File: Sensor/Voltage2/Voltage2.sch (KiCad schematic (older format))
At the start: 31 parts, among them J1 Conn_01x03_Female, J2 STX-3120-5B, J3 Conn_01x04_Female, T1 Transformer_1P_1S, U1 OPA4134

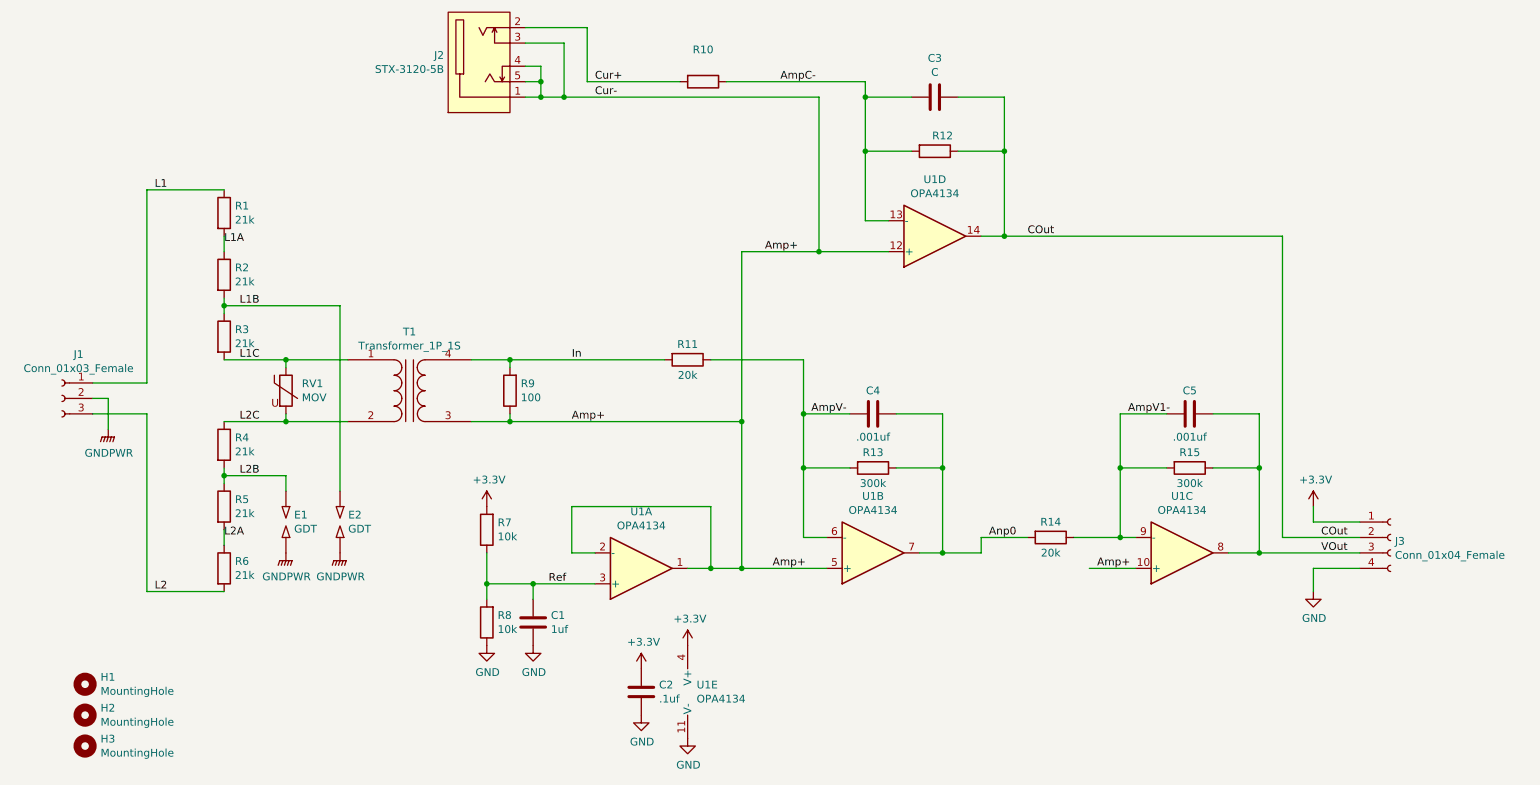
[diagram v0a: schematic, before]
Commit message: Fix footprint.  Fix wiring for connector.
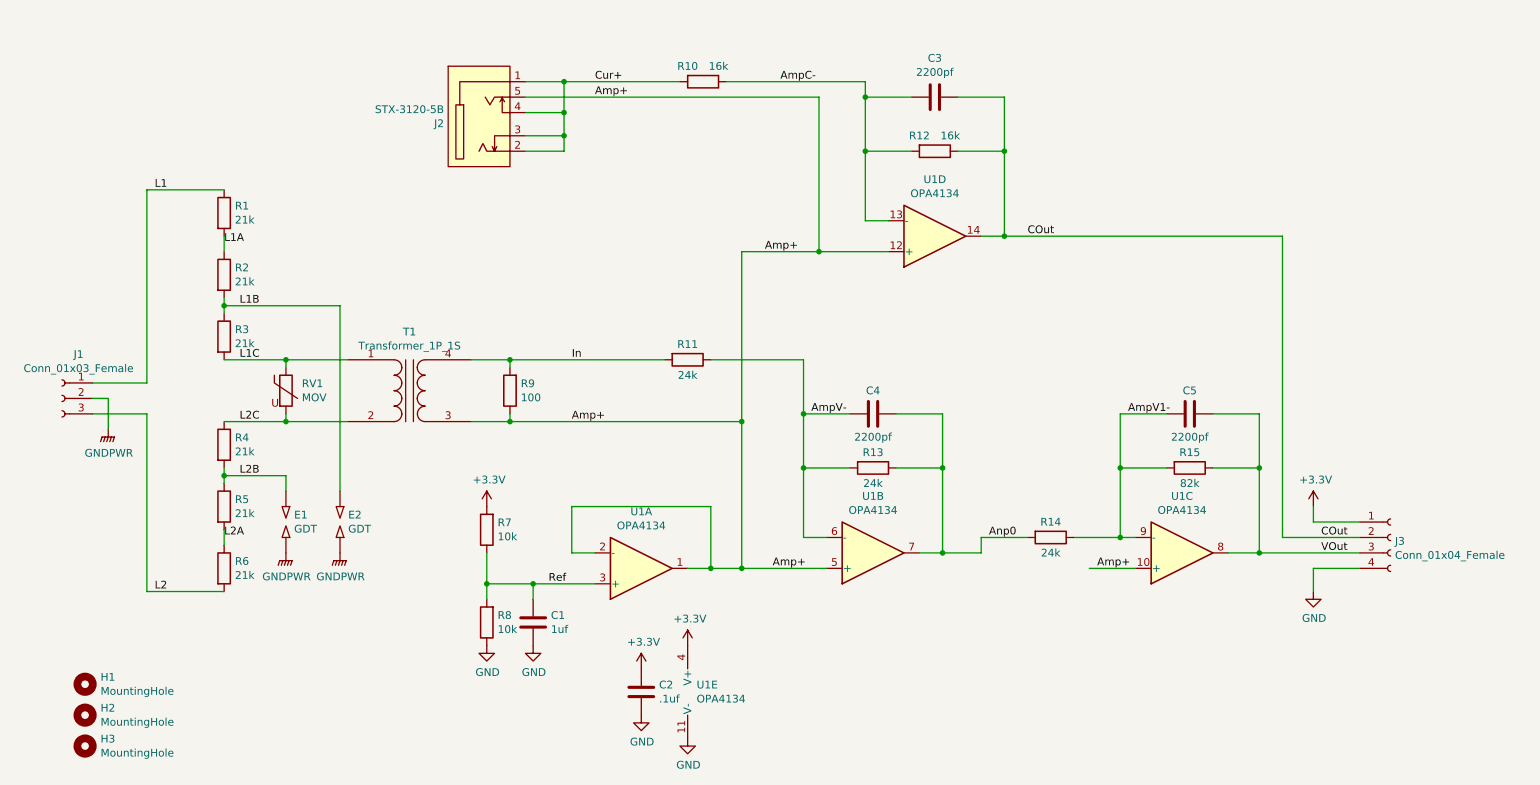
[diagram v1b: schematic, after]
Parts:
- C3: value C -> 2200pf
- C4, C5: value .001uf -> 2200pf
- R10, R12: value ~ -> 16k
- R11, R14: value 20k -> 24k
- R13: value 300k -> 24k
- R15: value 300k -> 82k
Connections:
- net Amp+: no longer J2.1, J2.3, J2.4
- net Cur+: now also J2.1, J2.3, J2.4
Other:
- moved on the sheet: J2
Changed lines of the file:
@@
 P 5600 4050
 F 0 "R11" V 5500 4050 50  0000 C CNN
-F 1 "20k" V 5700 4050 50  0000 C CNN
+F 1 "24k" V 5700 4050 50  0000 C CNN
 F 2 "Resistor_SMD:R_0805_2012Metric_Pad1.15x1.40mm_HandSolder" V 5530 4050 50  0001 C CNN
 F 3 "~" H 5600 4050 50  0001 C CNN
@@
 P 6800 4750
 F 0 "R13" V 6700 4750 50  0000 C CNN
-F 1 "300k" V 6900 4750 50  0000 C CNN
+F 1 "24k" V 6900 4750 50  0000 C CNN
 F 2 "Resistor_SMD:R_0805_2012Metric_Pad1.15x1.40mm_HandSolder" V 6730 4750 50  0001 C CNN
 F 3 "~" H 6800 4750 50  0001 C CNN
@@
 P 6800 4400
 F 0 "C4" V 6650 4400 50  0000 C CNN
-F 1 ".001uf" V 6950 4400 50  0000 C CNN
+F 1 "2200pf" V 6950 4400 50  0000 C CNN
 F 2 "Capacitor_SMD:C_0805_2012Metric_Pad1.15x1.40mm_HandSolder" H 6838 4250 50  0001 C CNN
 F 3 "~" H 6800 4400 50  0001 C CNN
@@
 U 1 1 5F724042
 P 7200 2700
-F 0 "R12" V 7100 2750 50  0000 C CNN
-F 1 "~" V 7100 2600 50  0000 C CNN
+F 0 "R12" V 7100 2600 50  0000 C CNN
+F 1 "16k" V 7100 2800 50  0000 C CNN
 F 2 "Resistor_SMD:R_0805_2012Metric_Pad1.15x1.40mm_HandSolder" V 7130 2700 50  0001 C CNN
 F 3 "~" H 7200 2700 50  0001 C CNN
@@
 U 1 1 5F724048
 P 5700 2250
-F 0 "R10" V 5493 2250 50  0000 C CNN
-F 1 "~" V 5584 2250 50  0000 C CNN
+F 0 "R10" V 5600 2150 50  0000 C CNN
+F 1 "16k" V 5600 2350 50  0000 C CNN
 F 2 "Resistor_SMD:R_0805_2012Metric_Pad1.15x1.40mm_HandSolder" V 5630 2250 50  0001 C CNN
 F 3 "~" H 5700 2250 50  0001 C CNN
@@
 P 7200 2350
 F 0 "C3" V 6948 2350 50  0000 C CNN
-F 1 "C" V 7039 2350 50  0000 C CNN
+F 1 "2200pf" V 7039 2350 50  0000 C CNN
 F 2 "Capacitor_SMD:C_0805_2012Metric_Pad1.15x1.40mm_HandSolder" H 7238 2200 50  0001 C CNN
 F 3 "~" H 7200 2350 50  0001 C CNN
@@
 Wire Wire Line
 	7350 2350 7650 2350
-$Comp
-L 00User:STX-3120-5B J2
-U 1 1 5F724079
-P 4300 2150
-F 0 "J2" H 4023 2079 50  0000 R CNN
-F 1 "STX-3120-5B" H 4023 2170 50  0000 R CNN
-F 2 "0MiscParts:AudioJack" H 4250 2600 50  0001 C CNN
-F 3 "" H 4250 2600 50  0001 C CNN
-	1    4300 2150
-	1    0    0    1
-$EndComp
-Wire Wire Line
-	4550 1900 4950 1900
-Wire Wire Line
-	4550 2150 4650 2150
 Text Label 5000 2250 0    50   ~ 0
 Cur+
 Text Label 5000 2350 0    50   ~ 0
-Cur-
+Amp+
 Text Label 6100 3350 0    50   ~ 0
 Amp+
@@
 P 8850 4750
 F 0 "R15" V 8750 4750 50  0000 C CNN
-F 1 "300k" V 8950 4750 50  0000 C CNN
+F 1 "82k" V 8950 4750 50  0000 C CNN
 F 2 "Resistor_SMD:R_0805_2012Metric_Pad1.15x1.40mm_HandSolder" V 8780 4750 50  0001 C CNN
 F 3 "~" H 8850 4750 50  0001 C CNN
@@
 P 8850 4400
 F 0 "C5" V 8700 4400 50  0000 C CNN
-F 1 ".001uf" V 9000 4400 50  0000 C CNN
+F 1 "2200pf" V 9000 4400 50  0000 C CNN
 F 2 "Capacitor_SMD:C_0805_2012Metric_Pad1.15x1.40mm_HandSolder" H 8888 4250 50  0001 C CNN
 F 3 "~" H 8850 4400 50  0001 C CNN
@@
 P 7950 5200
 F 0 "R14" V 7850 5200 50  0000 C CNN
-F 1 "20k" V 8050 5200 50  0000 C CNN
+F 1 "24k" V 8050 5200 50  0000 C CNN
 F 2 "Resistor_SMD:R_0805_2012Metric_Pad1.15x1.40mm_HandSolder" V 7880 5200 50  0001 C CNN
 F 3 "~" H 7950 5200 50  0001 C CNN
@@
 Wire Wire Line
 	3350 3700 3350 4900
-Wire Wire Line
-	4800 2000 4800 2350
-Wire Wire Line
-	4550 2000 4800 2000
-Connection ~ 4800 2350
-Wire Wire Line
-	4800 2350 6450 2350
-Wire Wire Line
-	4950 1900 4950 2250
-Wire Wire Line
-	4950 2250 5550 2250
-Wire Wire Line
-	4650 2150 4650 2250
-Wire Wire Line
-	4550 2350 4650 2350
-Connection ~ 4650 2350
-Wire Wire Line
-	4650 2350 4800 2350
-Wire Wire Line
-	4550 2250 4650 2250
-Connection ~ 4650 2250
-Wire Wire Line
-	4650 2250 4650 2350
 Text Label 2150 2950 0    50   ~ 0
 L1
@@
 Text Label 4850 4450 0    50   ~ 0
 Amp+
+$Comp
+L 00User:STX-3120-5B J2
+U 1 1 5F724079
+P 4300 2450
+F 0 "J2" H 4023 2379 50  0000 R CNN
+F 1 "STX-3120-5B" H 4023 2470 50  0000 R CNN
+F 2 "0MiscParts:AudioJack" H 4250 2900 50  0001 C CNN
+F 3 "" H 4250 2900 50  0001 C CNN
+	1    4300 2450
+	1    0    0    -1
+$EndComp
+Wire Wire Line
+	4550 2350 6450 2350
+Wire Wire Line
+	4550 2250 4800 2250
+Wire Wire Line
+	4550 2700 4800 2700
+Wire Wire Line
+	4800 2700 4800 2600
+Connection ~ 4800 2250
+Wire Wire Line
+	4800 2250 5550 2250
+Wire Wire Line
+	4550 2450 4800 2450
+Connection ~ 4800 2450
+Wire Wire Line
+	4800 2450 4800 2250
+Wire Wire Line
+	4550 2600 4800 2600
+Connection ~ 4800 2600
+Wire Wire Line
+	4800 2600 4800 2450
 $EndSCHEMATC
